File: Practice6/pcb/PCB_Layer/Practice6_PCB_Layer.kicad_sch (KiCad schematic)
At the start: 19 parts, among them J1 Conn_01x03, SW1 SW_1, SW2 SW_2, SW3 SW_3, SW4 SW_4, SW5 SW_5, SW6 SW_6, U1 ProMicro

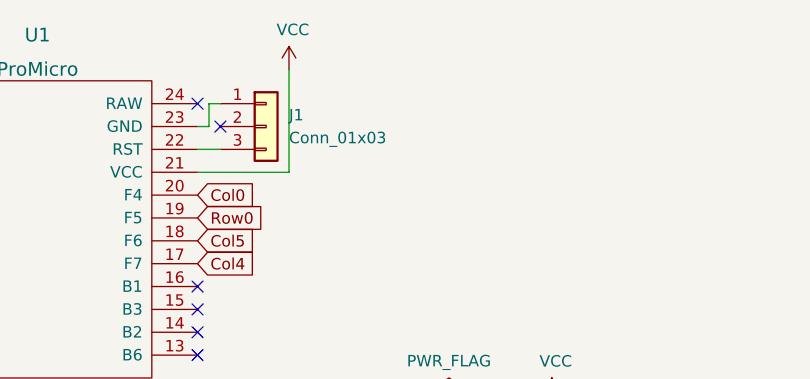
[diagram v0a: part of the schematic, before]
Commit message: fix: RST switch parts, hole position
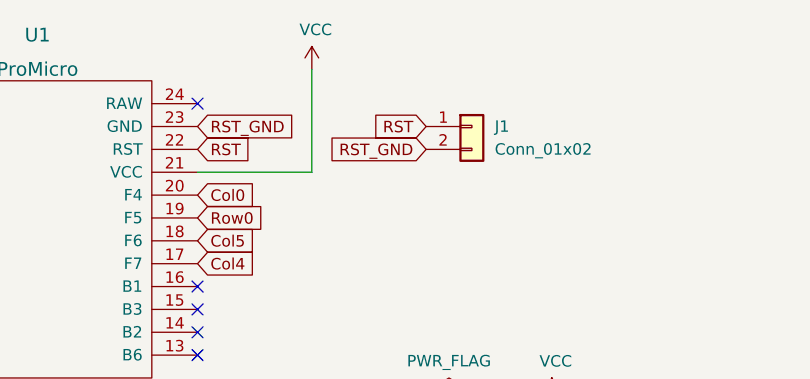
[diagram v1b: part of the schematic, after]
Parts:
- removed J1: Conn_01x03, Connector_PinHeader_2.54mm:PinHeader_1x03_P2.54mm_Vertical, symbol Connector_Generic:Conn_01x03
- added J1: Conn_01x02, akizukidenshi_parts:SW_108077_THDP07-060CB, symbol Connector_Generic:Conn_01x02
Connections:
- net RST_GND: now reaches U1.23 (GND)
- net RST_GND: now also J1.2 (Pin_2)
- net RST: now reaches U1.22 (RST)
- net RST: now also J1.1 (Pin_1)
- no-connect marks 14 -> 13
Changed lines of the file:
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@@
   (no_connect (at 118.11 57.15))
   (no_connect (at 82.55 39.37))
-  (no_connect (at 120.65 31.75))
   (no_connect (at 82.55 29.21))
   (no_connect (at 72.39 200.66))
@@
     (stroke (width 0) (type default) (color 0 0 0 0))
   )
-  (wire (pts (xy 128.27 36.83) (xy 128.27 25.4))
+  (wire (pts (xy 130.81 36.83) (xy 130.81 25.4))
     (stroke (width 0) (type default) (color 0 0 0 0))
   )
@@
     (stroke (width 0) (type default) (color 0 0 0 0))
   )
-  (wire (pts (xy 119.38 31.75) (xy 118.11 31.75))
-    (stroke (width 0) (type default) (color 0 0 0 0))
-  )
   (wire (pts (xy 105.41 114.3) (xy 107.95 114.3))
     (stroke (width 0) (type default) (color 0 0 0 0))
   )
-  (wire (pts (xy 118.11 36.83) (xy 128.27 36.83))
-    (stroke (width 0) (type default) (color 0 0 0 0))
-  )
-  (wire (pts (xy 120.65 29.21) (xy 119.38 29.21))
-    (stroke (width 0) (type default) (color 0 0 0 0))
-  )
-  (wire (pts (xy 119.38 29.21) (xy 119.38 31.75))
+  (wire (pts (xy 118.11 36.83) (xy 130.81 36.83))
     (stroke (width 0) (type default) (color 0 0 0 0))
   )
@@
   )
   (wire (pts (xy 59.69 121.92) (xy 77.47 121.92))
-    (stroke (width 0) (type default) (color 0 0 0 0))
-  )
-  (wire (pts (xy 120.65 34.29) (xy 118.11 34.29))
     (stroke (width 0) (type default) (color 0 0 0 0))
   )
@@
     )
   )
+  (global_label "RST" (shape input) (at 118.11 34.29 0) (fields_autoplaced)
+    (effects (font (size 1.27 1.27)) (justify left))
+    (property "Intersheet References" "${INTERSHEET_REFS}" (id 0) (at 123.8813 34.2106 0)
+      (effects (font (size 1.27 1.27)) (justify left) hide)
+    )
+  )
   (global_label "Col4" (shape input) (at 118.11 46.99 0) (fields_autoplaced)
     (effects (font (size 1.27 1.27)) (justify left))
@@
     (property "Intersheet References" "${INTERSHEET_REFS}" (id 0) (at 105.3306 96.252 90)
       (effects (font (size 1.27 1.27)) (justify left) hide)
+    )
+  )
+  (global_label "RST_GND" (shape input) (at 118.11 31.75 0) (fields_autoplaced)
+    (effects (font (size 1.27 1.27)) (justify left))
+    (property "Intersheet References" "${INTERSHEET_REFS}" (id 0) (at 128.7194 31.6706 0)
+      (effects (font (size 1.27 1.27)) (justify left) hide)
+    )
+  )
+  (global_label "RST" (shape input) (at 143.51 31.75 180) (fields_autoplaced)
+    (effects (font (size 1.27 1.27)) (justify right))
+    (property "Intersheet References" "${INTERSHEET_REFS}" (id 0) (at 137.7387 31.6706 0)
+      (effects (font (size 1.27 1.27)) (justify right) hide)
     )
   )
@@
     (property "Intersheet References" "${INTERSHEET_REFS}" (id 0) (at 64.6906 96.252 90)
       (effects (font (size 1.27 1.27)) (justify left) hide)
+    )
+  )
+  (global_label "RST_GND" (shape input) (at 143.51 34.29 180) (fields_autoplaced)
+    (effects (font (size 1.27 1.27)) (justify right))
+    (property "Intersheet References" "${INTERSHEET_REFS}" (id 0) (at 132.9006 34.2106 0)
+      (effects (font (size 1.27 1.27)) (justify right) hide)
     )
   )
@@
     (pin "4")
   )
-  (symbol (lib_id "Connector_Generic:Conn_01x03") (at 125.73 31.75 0) (unit 1)
-    (in_bom yes) (on_board yes) (fields_autoplaced)
-    (property "Reference" "J1" (id 0) (at 128.27 30.4799 0)
-      (effects (font (size 1.27 1.27)) (justify left))
-    )
-    (property "Value" "Conn_01x03" (id 1) (at 128.27 33.0199 0)
-      (effects (font (size 1.27 1.27)) (justify left))
-    )
-    (property "Footprint" "Connector_PinHeader_2.54mm:PinHeader_1x03_P2.54mm_Vertical" (id 2) (at 125.73 31.75 0)
-      (effects (font (size 1.27 1.27)) hide)
-    )
-    (property "Datasheet" "~" (id 3) (at 125.73 31.75 0)
-      (effects (font (size 1.27 1.27)) hide)
-    )
-    (pin "1")
-    (pin "2")
-    (pin "3")
-  )
   (symbol (lib_id "power:VCC") (at 157.48 62.23 0) (unit 1)
     (in_bom yes) (on_board yes)
@@
     )
   )
-  (symbol (lib_id "power:VCC") (at 128.27 25.4 0) (unit 1)
-    (in_bom yes) (on_board yes)
-    (property "Reference" "#PWR04" (id 0) (at 128.27 29.21 0)
-      (effects (font (size 1.27 1.27)) hide)
-    )
-    (property "Value" "VCC" (id 1) (at 128.7018 21.0058 0))
-    (property "Footprint" "" (id 2) (at 128.27 25.4 0)
-      (effects (font (size 1.27 1.27)) hide)
-    )
-    (property "Datasheet" "" (id 3) (at 128.27 25.4 0)
-      (effects (font (size 1.27 1.27)) hide)
-    )
-    (pin "1")
+  (symbol (lib_id "power:VCC") (at 130.81 25.4 0) (unit 1)
+    (in_bom yes) (on_board yes)
+    (property "Reference" "#PWR04" (id 0) (at 130.81 29.21 0)
+      (effects (font (size 1.27 1.27)) hide)
+    )
+    (property "Value" "VCC" (id 1) (at 131.2418 21.0058 0))
+    (property "Footprint" "" (id 2) (at 130.81 25.4 0)
+      (effects (font (size 1.27 1.27)) hide)
+    )
+    (property "Datasheet" "" (id 3) (at 130.81 25.4 0)
+      (effects (font (size 1.27 1.27)) hide)
+    )
+    (pin "1")
+  )
+  (symbol (lib_id "Connector_Generic:Conn_01x02") (at 148.59 31.75 0) (unit 1)
+    (in_bom yes) (on_board yes) (fields_autoplaced)
+    (property "Reference" "J1" (id 0) (at 151.13 31.7499 0)
+      (effects (font (size 1.27 1.27)) (justify left))
+    )
+    (property "Value" "Conn_01x02" (id 1) (at 151.13 34.2899 0)
+      (effects (font (size 1.27 1.27)) (justify left))
+    )
+    (property "Footprint" "akizukidenshi_parts:SW_108077_THDP07-060CB" (id 2) (at 148.59 31.75 0)
+      (effects (font (size 1.27 1.27)) hide)
+    )
+    (property "Datasheet" "~" (id 3) (at 148.59 31.75 0)
+      (effects (font (size 1.27 1.27)) hide)
+    )
+    (pin "1")
+    (pin "2")
   )
   (symbol (lib_id "power:PWR_FLAG") (at 146.05 62.23 0) (unit 1)
@@
       (reference "H7") (unit 1) (value "MountingHole") (footprint "kbd_Hole:m2_Screw_Hole")
     )
-    (path "/09caf31d-cc43-432b-8d70-26d907312904"
-      (reference "J1") (unit 1) (value "Conn_01x03") (footprint "Connector_PinHeader_2.54mm:PinHeader_1x03_P2.54mm_Vertical")
+    (path "/b2436b50-0c49-49c5-a436-820d80475b19"
+      (reference "J1") (unit 1) (value "Conn_01x02") (footprint "akizukidenshi_parts:SW_108077_THDP07-060CB")
     )
     (path "/624a8854-374a-4944-b4a8-193bf0e1a89e"
